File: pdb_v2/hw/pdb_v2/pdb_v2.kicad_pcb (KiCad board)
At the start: 4 copper layers, 95.9 x 35.1 mm, 80 parts, among them J1 XT30-M_Ver, J2 JST-PH_01x02, J3 JST-PH_01x02, J4 JST-PH_01x02, J5 JST-PH_01x02, Q1 60Vds, U1 LMR51635XFDDCR, U2 AP63205WU-7, U3 AP63203WU-7

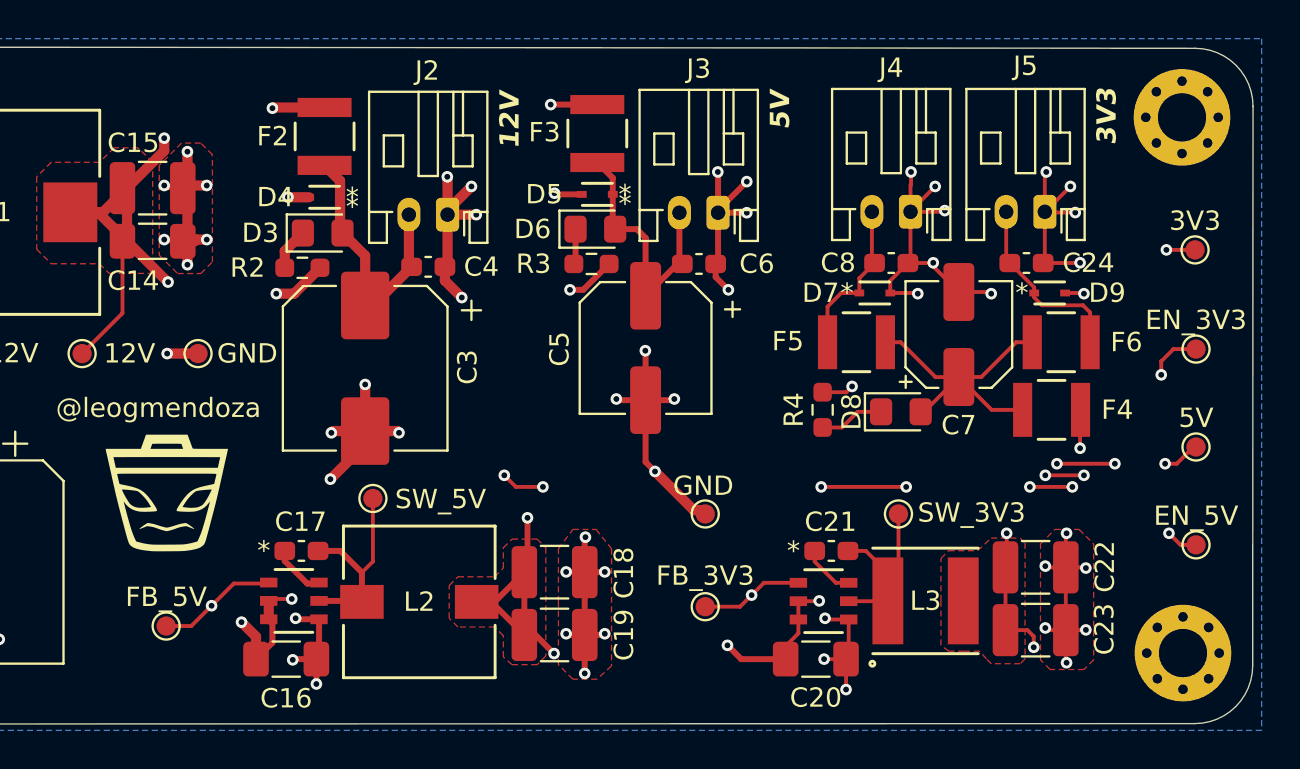
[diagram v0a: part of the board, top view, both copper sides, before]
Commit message: Removed 12V to 5V stage
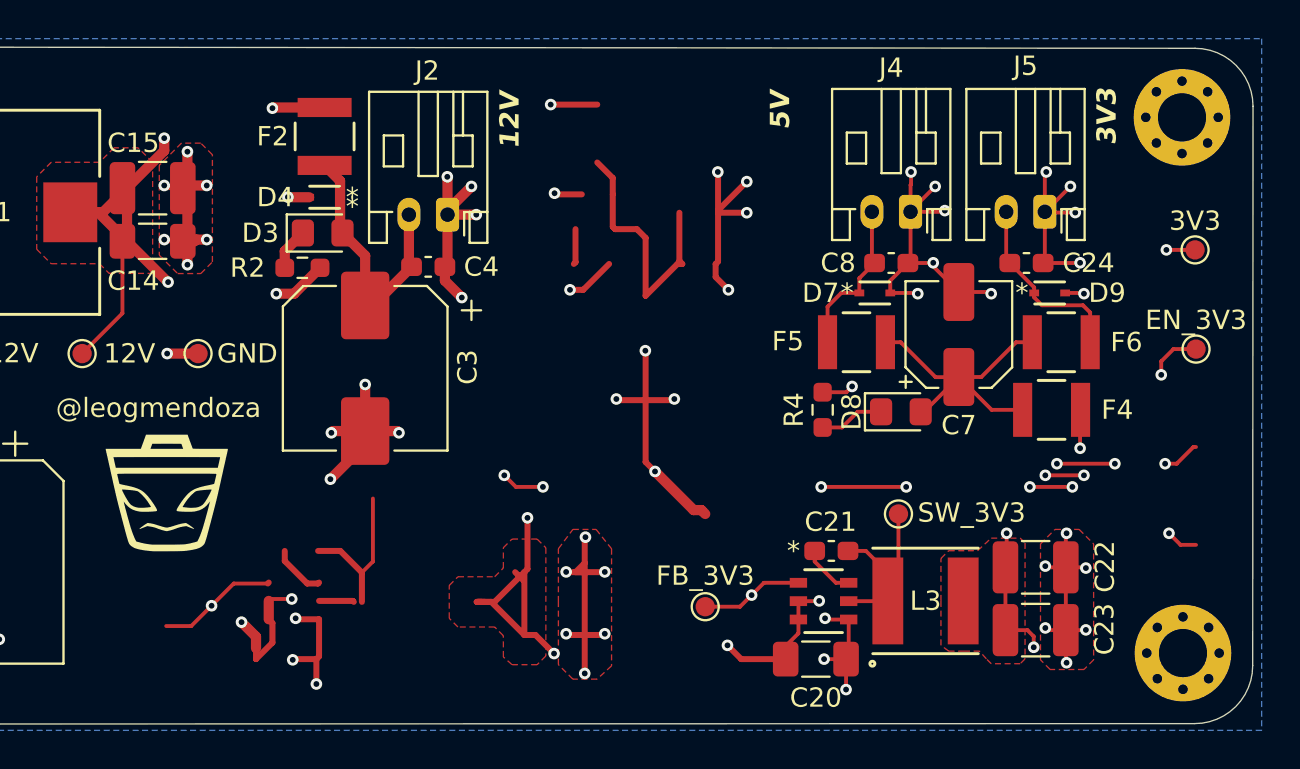
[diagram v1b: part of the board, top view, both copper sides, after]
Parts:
- removed 5V1: 5V, test_point_custom:TestPoint_Pad_D1.0mm
- removed C16: 10uF, Capacitor_SMD:C_1206_3216Metric_Pad1.33x1.80mm_HandSolder
- removed C17, C6: 0.1uF, Capacitor_SMD:C_0603_1608Metric_Pad1.08x0.95mm_HandSolder
- removed C18, C19: 22uF, Capacitor_SMD:C_1210_3225Metric_Pad1.33x2.70mm_HandSolder
- removed C5: 47uF, Capacitor_SMD:CP_Elec_6.3x7.7
- removed D5: 5Vrwm, ESD5Z5.0T1G:SOD-523_0P9X1P3_ONS
- removed D6: 2Vf, LED_SMD:LED_0805_2012Metric_Pad1.15x1.40mm_HandSolder
- removed EN_5V1: EN_5V, test_point_custom:TestPoint_Pad_D1.0mm
- removed F3: 0.5A 16V, 0ZCH0050FF2G:0ZCH_BEL
- removed FB_5V1: FB_5V, test_point_custom:TestPoint_Pad_D1.0mm
- removed GND3: GND, test_point_custom:TestPoint_Pad_D1.0mm
- removed J3: JST-PH_01x02, Connector_JST:JST_PH_S2B-PH-K_1x02_P2.00mm_Horizontal
- removed L2: 4.7uH, 7447779004:IND_7345R_WE-PD_WRE
- removed R3: 1.5k, Resistor_SMD:R_0603_1608Metric_Pad0.98x0.95mm_HandSolder
- removed SW_5V1: SW_5V, test_point_custom:TestPoint_Pad_D1.0mm
- removed U2: AP63205WU-7, AP63205WU-7:SOIC_05WU-7_DIO
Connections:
- C20 pad 1: 5V_BUS -> 12V_BUS
- EN_3V3 pad 1: 5V_BUS -> 12V_BUS
- U3 pad 2: 5V_BUS -> 12V_BUS
- U3 pad 3: 5V_BUS -> 12V_BUS
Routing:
- net 5V_BUS: track 145.5 -> 0.00 mm, vias 12 -> 0
- net 12V_BUS: track 135.5 -> 281.0 mm, vias 13 -> 25
- net (no net): track 0.00 -> 28.7 mm
- net Net-(D6-A): track 13.9 -> 0.00 mm
- net Net-(U2-SW): track 10.1 -> 0.00 mm
- net Net-(U2-BST): track 2.80 -> 0.00 mm
- net Net-(D6-K): track 1.84 -> 0.00 mm
- removed copper zone on F.Cu, net 5V_BUS

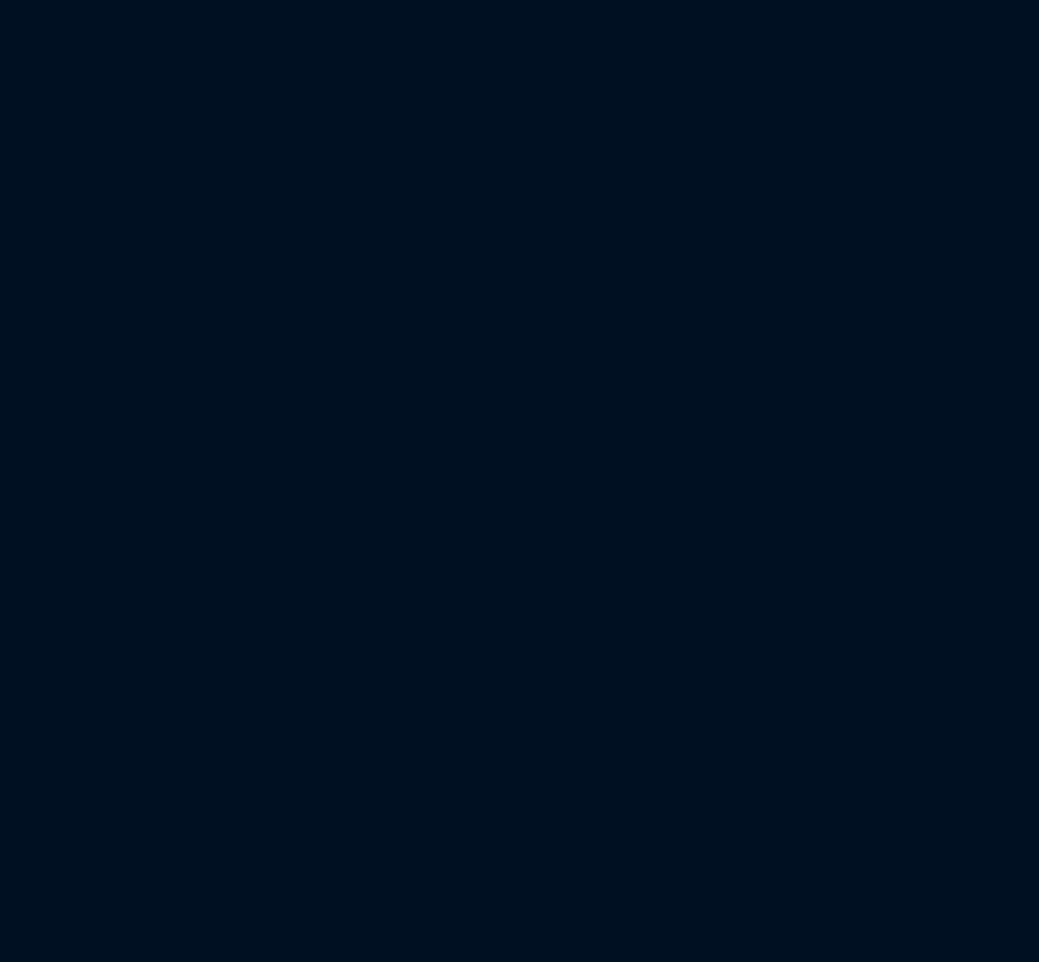
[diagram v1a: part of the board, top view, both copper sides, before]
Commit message: Added footprints
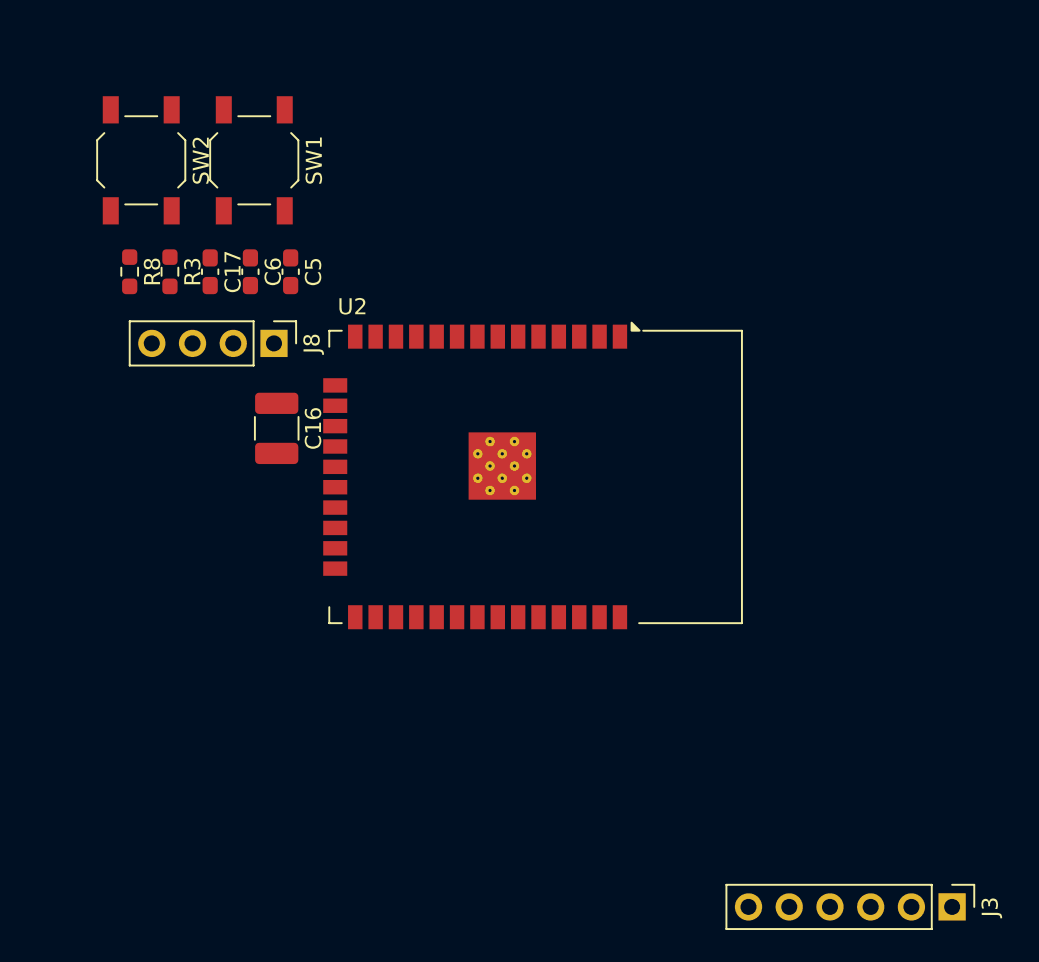
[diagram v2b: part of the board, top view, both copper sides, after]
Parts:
- added C16: 22uF, Capacitor_SMD:C_1210_3225Metric_Pad1.33x2.70mm_HandSolder, F.Cu at (129.8, 41.7)
- added C17: 0.1uF, Capacitor_SMD:C_0603_1608Metric_Pad1.08x0.95mm_HandSolder, F.Cu at (125.6, 31.9)
- added C5: 0.1uF, Capacitor_SMD:C_0603_1608Metric_Pad1.08x0.95mm_HandSolder, F.Cu at (130.6, 31.9)
- added C6: 0.1uF, Capacitor_SMD:C_0603_1608Metric_Pad1.08x0.95mm_HandSolder, F.Cu at (128.1, 31.9)
- added J3: Conn_01x06_Pin, Connector_PinHeader_2.54mm:PinHeader_1x06_P2.54mm_Vertical, F.Cu at (171.9, 71.6)
- added J8: Conn_01x04, Connector_PinHeader_2.54mm:PinHeader_1x04_P2.54mm_Vertical, F.Cu at (129.6, 36.4)
- added R3: 10k, Resistor_SMD:R_0603_1608Metric_Pad0.98x0.95mm_HandSolder, F.Cu at (123.1, 31.9)
- added R8: 10k, Resistor_SMD:R_0603_1608Metric_Pad0.98x0.95mm_HandSolder, F.Cu at (120.6, 31.9)
- added SW1: SW_Push, Button_Switch_SMD:SW_SPST_TL3342, F.Cu at (128.3, 25.0)
- added SW2: SW_Push, Button_Switch_SMD:SW_SPST_TL3342, F.Cu at (121.3, 25.0)
- added U2: ESP32-WROOM-32, RF_Module:ESP32-WROOM-32, F.Cu at (142.9, 44.8)

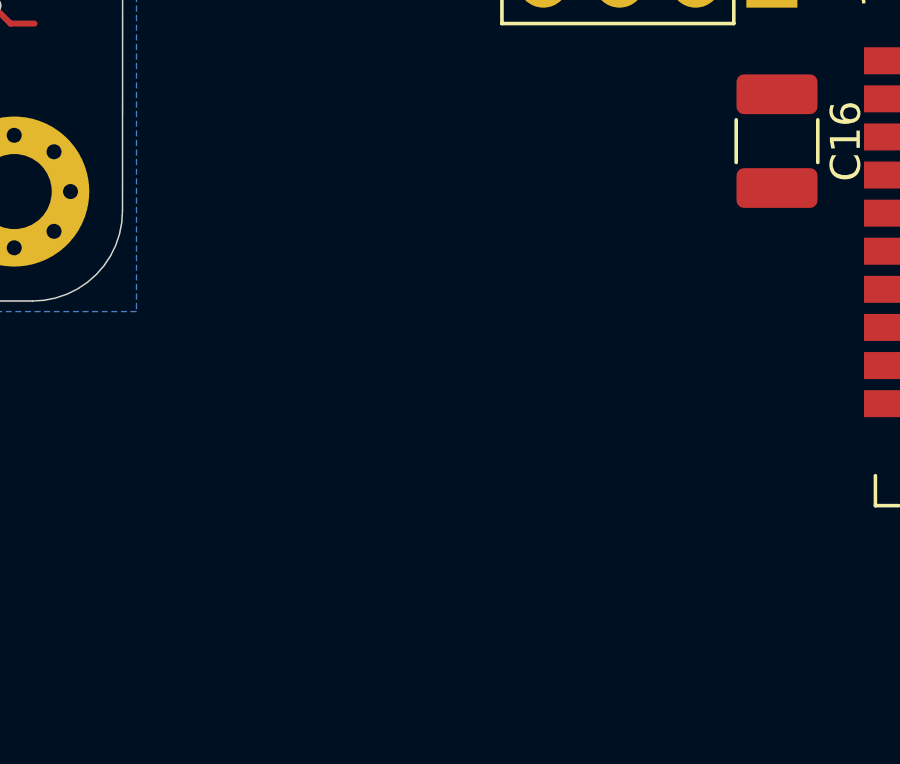
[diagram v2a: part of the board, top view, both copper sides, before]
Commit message: added footprints for connectors
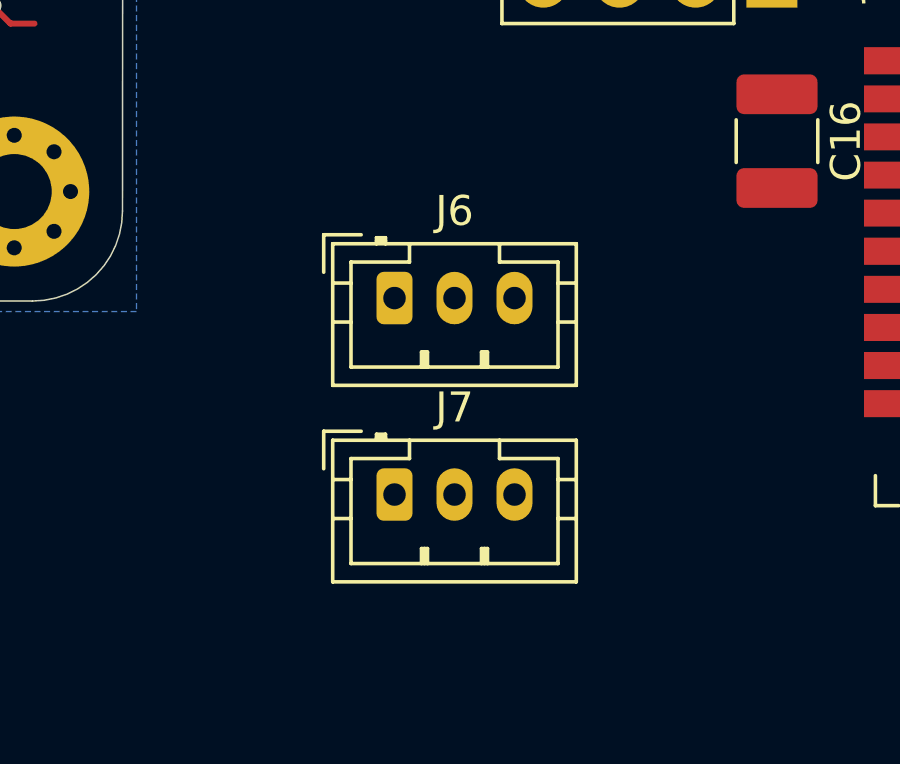
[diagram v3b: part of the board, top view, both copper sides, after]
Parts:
- added J6: Conn_01x03, Connector_JST:JST_PH_B3B-PH-K_1x03_P2.00mm_Vertical, F.Cu at (117.0, 47.0)
- added J7: Conn_01x03, Connector_JST:JST_PH_B3B-PH-K_1x03_P2.00mm_Vertical, F.Cu at (117.0, 53.5)

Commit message: PCB cleaned
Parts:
- moved U2 88.7 mm to (55.2, 58.4), turned to 180 degrees
- moved H3 21.6 mm to (15.2, 65.0)
- moved H4 21.6 mm to (105.0, 65.0)
- moved J8 7.08 mm to (122.8, 38.5)
- moved R8 6.08 mm to (114.5, 31.9)
- moved R3 3.59 mm to (119.5, 31.9)
- moved C17 2.10 mm to (123.5, 31.9)
- moved C5 1.88 mm to (132.5, 31.9)
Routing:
- net GND: track 189.5 -> 156.4 mm, vias 83 -> 70
- net (no net): track 28.7 -> 0.00 mm
- net 12V_BUS: track 281.0 -> 256.5 mm, vias 25 -> 22
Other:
- board size 95.9 x 35.1 mm -> 95.9 x 56 mm

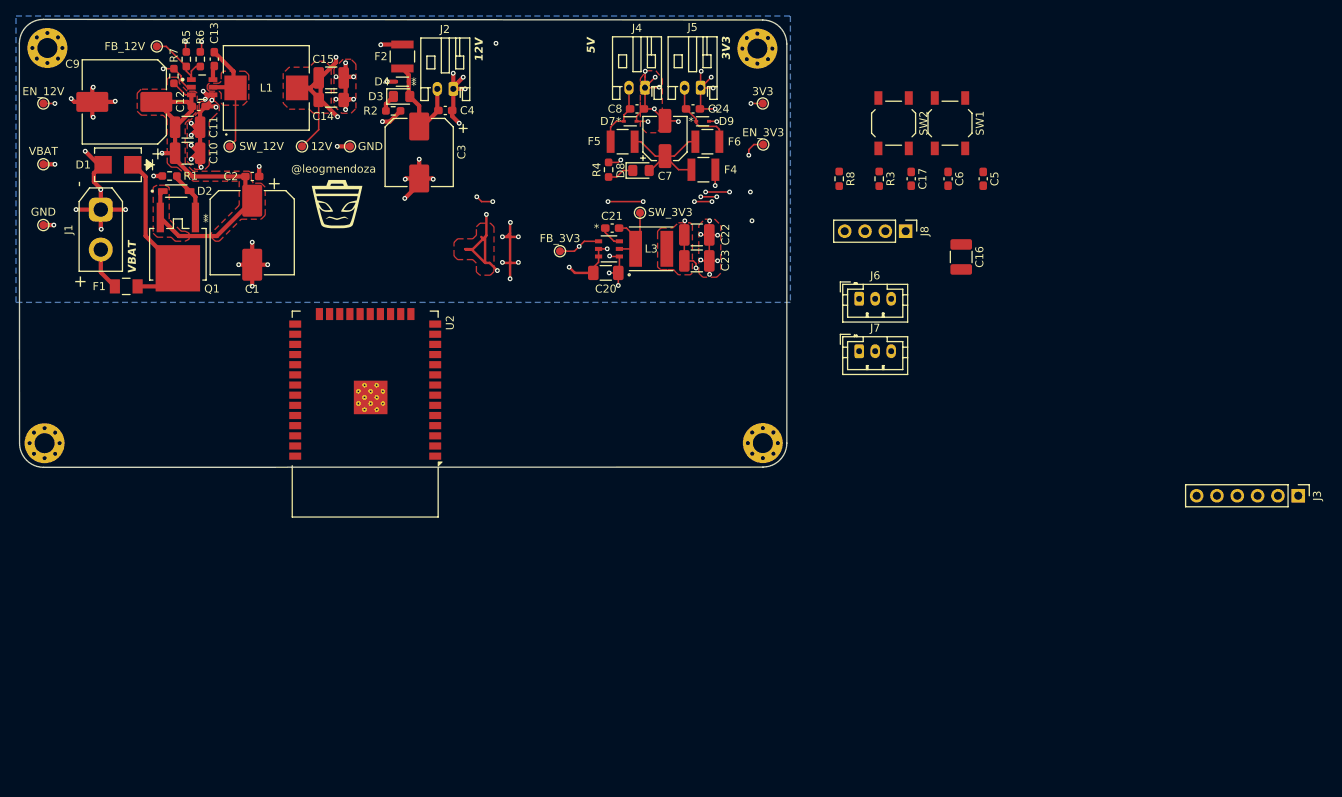
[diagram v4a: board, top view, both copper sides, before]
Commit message: cleaned up, added oled footprint, arranged some components
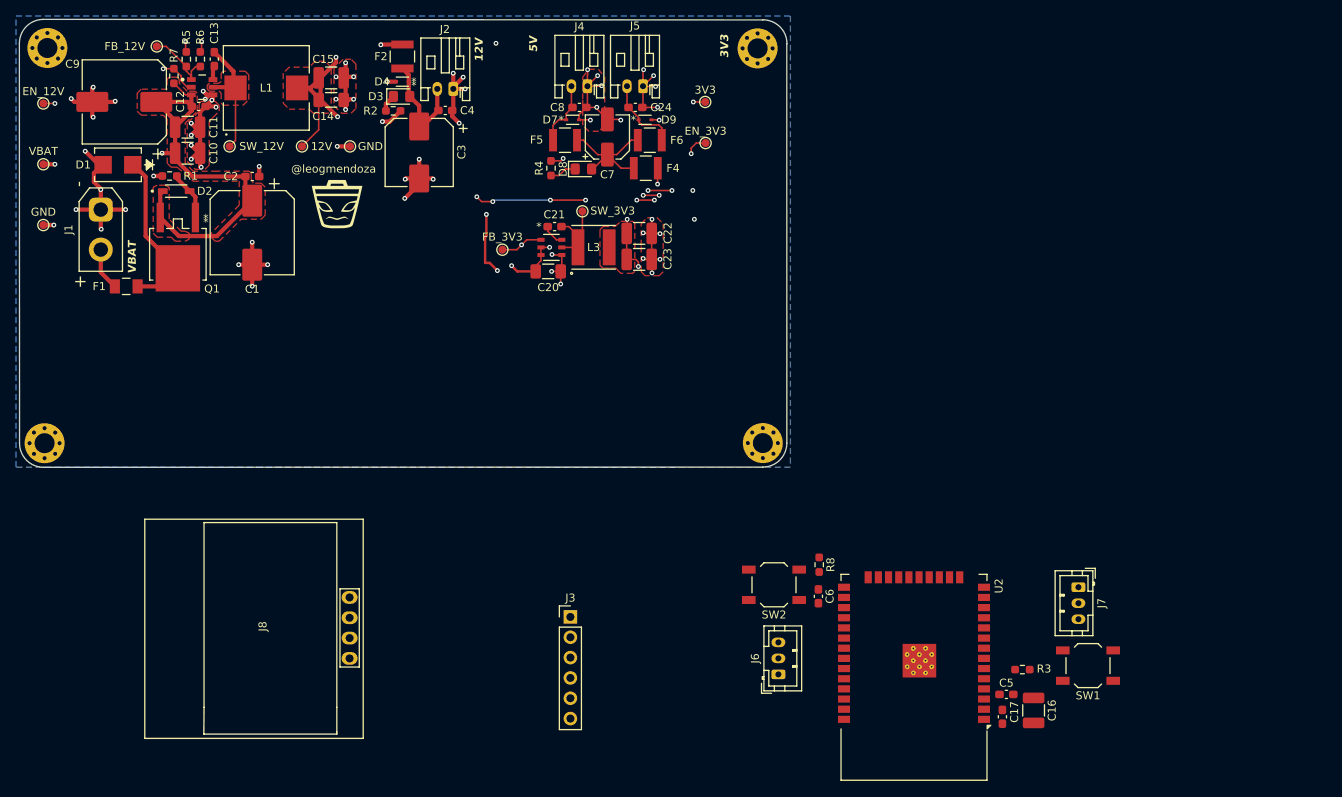
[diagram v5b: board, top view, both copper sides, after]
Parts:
- J8: footprint Connector_PinHeader_2.54mm:PinHeader_1x04_P2.54mm_Vertical -> SSD1306:128x64OLED
- moved J8 94.1 mm to (42.7, 87.9)
- moved J3 92.2 mm to (80.9, 86.7), turned to 0 degrees
- moved U2 76.1 mm to (123.8, 91.3)
- moved SW1 70.0 mm to (145.6, 92.8), turned to 180 degrees
- moved C17 68.2 mm to (134.9, 99.2)
- moved C5 64.5 mm to (135.4, 96.4), turned to 0 degrees
- moved R3 63.9 mm to (137.4, 93.3), turned to 180 degrees
- moved SW2 59.6 mm to (106.3, 82.7), turned to 180 degrees
- moved C16 57.4 mm to (138.8, 98.4)
- moved C6 54.6 mm to (111.9, 84.1)
- moved R8 48.3 mm to (112.0, 80.2)
- moved J6 48.0 mm to (106.9, 93.9), turned to 90 degrees
- moved J7 40.3 mm to (144.4, 83.0), turned to -90 degrees
- moved 3V3 7.20 mm to (97.8, 22.3)
- moved C20 7.20 mm to (78.1, 43.5)
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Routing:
- net 12V_BUS: track 256.5 -> 205.2 mm
- net GND: track 156.4 -> 144.3 mm, vias 70 -> 64
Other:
- board size 95.9 x 56 mm -> 96 x 56 mm
